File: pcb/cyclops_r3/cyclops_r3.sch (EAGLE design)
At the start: 78 parts, among them Q1 SUM11006, Q2 IRF510, U1 MCP4921, U2 317-N, U3 TLV37, U4 337-N, U5 ADR03, U6 OP1177, U7 TLV2374, U8 ZXTD45

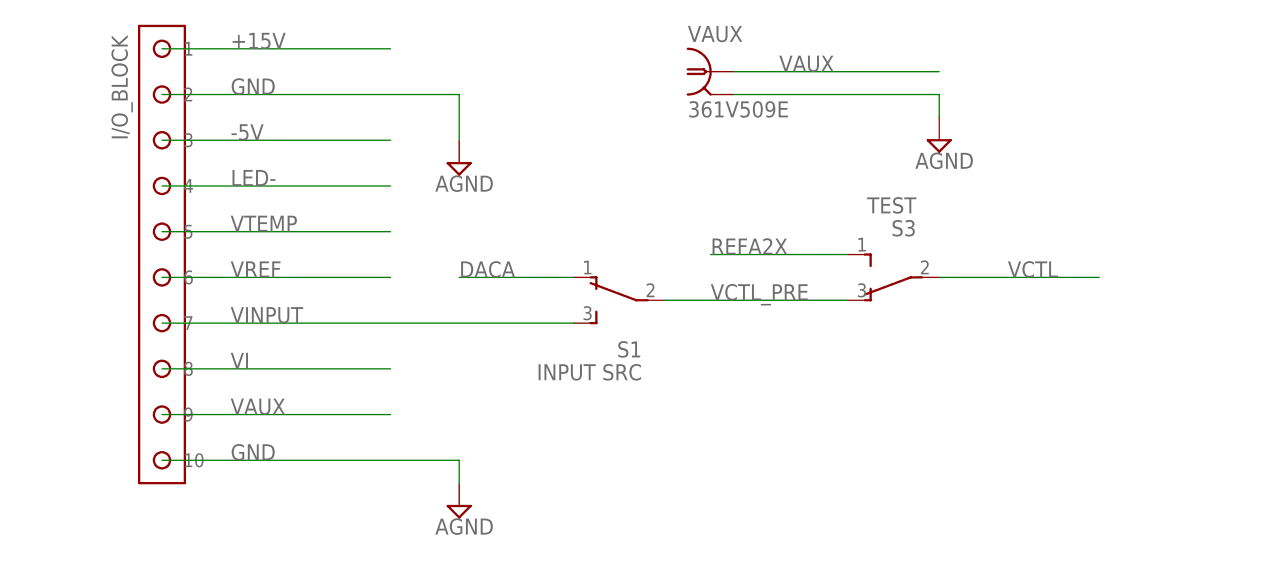
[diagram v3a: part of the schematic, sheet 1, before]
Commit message: Almost done fixing the top/bottom side I/O labels. Also, found a big mistake in the 10-pin screw terminal header: I replaced the +LED supply with the -5V supply rail. I had to shift all the pins to get that LED pin back and I have not finished rerouting the board.
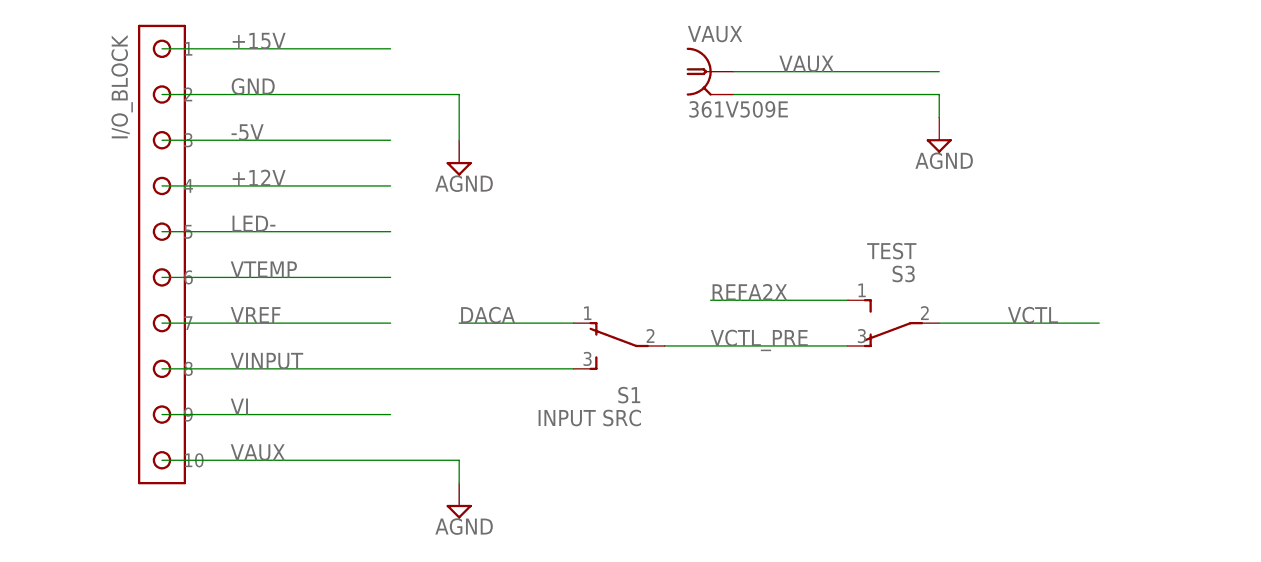
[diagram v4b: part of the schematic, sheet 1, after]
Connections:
- net +12V: now also I/O_BLOCK.4
- net GND: no longer I/O_BLOCK.10
- net LED-: now also I/O_BLOCK.5; no longer I/O_BLOCK.4
- net VAUX: now also I/O_BLOCK.10; no longer I/O_BLOCK.9
- net VI: now also I/O_BLOCK.9; no longer I/O_BLOCK.8
- net VINPUT: now also I/O_BLOCK.8; no longer I/O_BLOCK.7
- net VREF: now also I/O_BLOCK.7; no longer I/O_BLOCK.6
- net VTEMP: now also I/O_BLOCK.6; no longer I/O_BLOCK.5
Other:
- moved on the sheet: S1, S3
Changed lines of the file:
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@@
 <instance part="SUPPLY32" gate="G$1" x="76.2" y="-17.78"/>
 <instance part="SUPPLY33" gate="G$1" x="76.2" y="-55.88"/>
-<instance part="S1" gate="G$1" x="96.52" y="-33.02" rot="MR0"/>
+<instance part="S1" gate="G$1" x="96.52" y="-38.1" rot="MR0"/>
 <instance part="SUPPLY12" gate="G$1" x="165.1" y="22.86"/>
 <instance part="SUPPLY34" gate="PE" x="139.7" y="22.86"/>
-<instance part="S3" gate="G$1" x="127" y="-30.48" rot="R180"/>
+<instance part="S3" gate="G$1" x="127" y="-35.56" rot="R180"/>
 <instance part="SUPPLY4" gate="PE" x="60.96" y="10.16"/>
 <instance part="SUPPLY29" gate="PE" x="38.1" y="83.82"/>
@@
 <segment>
 <pinref part="S1" gate="G$1" pin="1"/>
-<wire x1="76.2" y1="-30.48" x2="88.9" y2="-30.48" width="0.1524" layer="91"/>
-<label x="76.2" y="-30.48" size="1.778" layer="95"/>
+<wire x1="76.2" y1="-35.56" x2="88.9" y2="-35.56" width="0.1524" layer="91"/>
+<label x="76.2" y="-35.56" size="1.778" layer="95"/>
 </segment>
 </net>
@@
 <net name="LED-" class="0">
 <segment>
-<pinref part="I/O_BLOCK" gate="G$1" pin="4"/>
-<wire x1="43.18" y1="-20.32" x2="68.58" y2="-20.32" width="0.1524" layer="91"/>
-<label x="50.8" y="-20.32" size="1.778" layer="95"/>
+<pinref part="I/O_BLOCK" gate="G$1" pin="5"/>
+<wire x1="43.18" y1="-25.4" x2="68.58" y2="-25.4" width="0.1524" layer="91"/>
+<label x="50.8" y="-25.4" size="1.778" layer="95"/>
 </segment>
 </net>
@@
 </segment>
 <segment>
-<pinref part="I/O_BLOCK" gate="G$1" pin="10"/>
-<wire x1="43.18" y1="-50.8" x2="76.2" y2="-50.8" width="0.1524" layer="91"/>
-<pinref part="SUPPLY33" gate="G$1" pin="AGND"/>
-<wire x1="76.2" y1="-50.8" x2="76.2" y2="-53.34" width="0.1524" layer="91"/>
-<label x="50.8" y="-50.8" size="1.778" layer="95"/>
-</segment>
-<segment>
 <pinref part="C1" gate="C" pin="2"/>
 <pinref part="SUPPLY16" gate="G$1" pin="AGND"/>
@@
 <net name="VAUX" class="0">
 <segment>
+<pinref part="VAUX" gate="G$1" pin="1"/>
+<wire x1="106.68" y1="-7.62" x2="129.54" y2="-7.62" width="0.1524" layer="91"/>
+<label x="111.76" y="-7.62" size="1.778" layer="95"/>
+</segment>
+<segment>
+<pinref part="I/O_BLOCK" gate="G$1" pin="10"/>
+<wire x1="43.18" y1="-50.8" x2="76.2" y2="-50.8" width="0.1524" layer="91"/>
+<pinref part="SUPPLY33" gate="G$1" pin="AGND"/>
+<wire x1="76.2" y1="-50.8" x2="76.2" y2="-53.34" width="0.1524" layer="91"/>
+<label x="50.8" y="-50.8" size="1.778" layer="95"/>
+</segment>
+</net>
+<net name="VI" class="0">
+<segment>
 <pinref part="I/O_BLOCK" gate="G$1" pin="9"/>
 <wire x1="43.18" y1="-45.72" x2="68.58" y2="-45.72" width="0.1524" layer="91"/>
 <label x="50.8" y="-45.72" size="1.778" layer="95"/>
 </segment>
-<segment>
-<pinref part="VAUX" gate="G$1" pin="1"/>
-<wire x1="106.68" y1="-7.62" x2="129.54" y2="-7.62" width="0.1524" layer="91"/>
-<label x="111.76" y="-7.62" size="1.778" layer="95"/>
-</segment>
-</net>
-<net name="VI" class="0">
+</net>
+<net name="VINPUT" class="0">
 <segment>
 <pinref part="I/O_BLOCK" gate="G$1" pin="8"/>
-<wire x1="43.18" y1="-40.64" x2="68.58" y2="-40.64" width="0.1524" layer="91"/>
+<wire x1="43.18" y1="-40.64" x2="88.9" y2="-40.64" width="0.1524" layer="91"/>
 <label x="50.8" y="-40.64" size="1.778" layer="95"/>
-</segment>
-</net>
-<net name="VINPUT" class="0">
-<segment>
-<pinref part="I/O_BLOCK" gate="G$1" pin="7"/>
-<label x="50.8" y="-35.56" size="1.778" layer="95"/>
 <pinref part="S1" gate="G$1" pin="3"/>
-<wire x1="43.18" y1="-35.56" x2="88.9" y2="-35.56" width="0.1524" layer="91"/>
 </segment>
 </net>
@@
 <net name="VTEMP" class="0">
 <segment>
-<pinref part="I/O_BLOCK" gate="G$1" pin="5"/>
-<wire x1="43.18" y1="-25.4" x2="68.58" y2="-25.4" width="0.1524" layer="91"/>
-<label x="50.8" y="-25.4" size="1.778" layer="95"/>
+<pinref part="I/O_BLOCK" gate="G$1" pin="6"/>
+<wire x1="43.18" y1="-30.48" x2="68.58" y2="-30.48" width="0.1524" layer="91"/>
+<label x="50.8" y="-30.48" size="1.778" layer="95"/>
 </segment>
 </net>
@@
 <net name="VCTL_PRE" class="0">
 <segment>
-<wire x1="99.06" y1="-33.02" x2="119.38" y2="-33.02" width="0.1524" layer="91"/>
+<wire x1="99.06" y1="-38.1" x2="119.38" y2="-38.1" width="0.1524" layer="91"/>
 <pinref part="S1" gate="G$1" pin="2"/>
+<label x="104.14" y="-38.1" size="1.778" layer="95"/>
+<pinref part="S3" gate="G$1" pin="1"/>
+</segment>
+</net>
+<net name="VCTL" class="0">
+<segment>
+<pinref part="S3" gate="G$1" pin="2"/>
+<wire x1="129.54" y1="-35.56" x2="147.32" y2="-35.56" width="0.1524" layer="91"/>
+<label x="137.16" y="-35.56" size="1.778" layer="95"/>
+</segment>
+</net>
+<net name="REFA2X" class="0">
+<segment>
+<pinref part="S3" gate="G$1" pin="3"/>
+<wire x1="119.38" y1="-33.02" x2="104.14" y2="-33.02" width="0.1524" layer="91"/>
 <label x="104.14" y="-33.02" size="1.778" layer="95"/>
-<pinref part="S3" gate="G$1" pin="1"/>
-</segment>
-</net>
-<net name="VCTL" class="0">
-<segment>
-<pinref part="S3" gate="G$1" pin="2"/>
-<wire x1="129.54" y1="-30.48" x2="147.32" y2="-30.48" width="0.1524" layer="91"/>
-<label x="137.16" y="-30.48" size="1.778" layer="95"/>
-</segment>
-</net>
-<net name="REFA2X" class="0">
-<segment>
-<pinref part="S3" gate="G$1" pin="3"/>
-<wire x1="119.38" y1="-27.94" x2="104.14" y2="-27.94" width="0.1524" layer="91"/>
-<label x="104.14" y="-27.94" size="1.778" layer="95"/>
 </segment>
 </net>
 <net name="VREF" class="0">
 <segment>
-<pinref part="I/O_BLOCK" gate="G$1" pin="6"/>
-<wire x1="43.18" y1="-30.48" x2="68.58" y2="-30.48" width="0.1524" layer="91"/>
-<label x="50.8" y="-30.48" size="1.778" layer="95"/>
+<wire x1="43.18" y1="-35.56" x2="68.58" y2="-35.56" width="0.1524" layer="91"/>
+<pinref part="I/O_BLOCK" gate="G$1" pin="7"/>
+<label x="50.8" y="-35.56" size="1.778" layer="95"/>
 </segment>
 </net>
@@
 </segment>
 </net>
+<net name="+12V" class="1">
+<segment>
+<pinref part="I/O_BLOCK" gate="G$1" pin="4"/>
+<wire x1="43.18" y1="-20.32" x2="68.58" y2="-20.32" width="0.1524" layer="91"/>
+<label x="50.8" y="-20.32" size="1.778" layer="95"/>
+</segment>
+</net>

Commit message: Board sent to fab house. Doing some directory clean up now.
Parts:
- Q2: value IRF510 -> IRF540
- S4: value UNKILL -> REVIVE
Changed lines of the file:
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@@
 <part name="I/O_BLOCK" library="cyclops" deviceset="SCREW10" device="_0.1-THRU"/>
 <part name="SUPPLY32" library="cyclops" deviceset="AGND" device=""/>
-<part name="SUPPLY33" library="cyclops" deviceset="AGND" device=""/>
 <part name="S1" library="cyclops" deviceset="SPDT" device="_PCM12" value="INPUT SRC"/>
 <part name="C17" library="cyclops" deviceset="C" device="_0603" value=".1uF"/>
@@
 <part name="U8" library="cyclops" deviceset="ZXTD4591E6" device="" value="ZXTD45"/>
 <part name="SUPPLY35" library="cyclops" deviceset="AGND" device=""/>
-<part name="Q2" library="cyclops" deviceset="N-MOSFET" device="TO-262" value="IRF510"/>
+<part name="Q2" library="cyclops" deviceset="N-MOSFET" device="TO-262" value="IRF540"/>
 <part name="R23" library="cyclops" deviceset="R" device="_0603" value="10"/>
 <part name="R24" library="cyclops" deviceset="R" device="_0603" value="1k"/>
@@
 <part name="C5" library="cyclops" deviceset="C" device="_0603" value="10nF"/>
 <part name="SUPPLY45" library="cyclops" deviceset="AGND" device=""/>
-<part name="S4" library="cyclops" deviceset="SPST_TACT" device="-EVQQ2" value="UNKILL"/>
+<part name="S4" library="cyclops" deviceset="SPST_TACT" device="-EVQQ2" value="REVIVE"/>
 <part name="SUPPLY46" library="supply2" deviceset="AGND" device=""/>
 <part name="U4" library="cyclops" deviceset="*337" device="IMP" value="337-N"/>
@@
 </instance>
 <instance part="SUPPLY32" gate="G$1" x="76.2" y="-17.78"/>
-<instance part="SUPPLY33" gate="G$1" x="76.2" y="-55.88"/>
 <instance part="S1" gate="G$1" x="96.52" y="-38.1" rot="MR0"/>
 <instance part="SUPPLY12" gate="G$1" x="165.1" y="22.86"/>
@@
 <segment>
 <pinref part="I/O_BLOCK" gate="G$1" pin="10"/>
-<wire x1="43.18" y1="-50.8" x2="76.2" y2="-50.8" width="0.1524" layer="91"/>
-<pinref part="SUPPLY33" gate="G$1" pin="AGND"/>
-<wire x1="76.2" y1="-50.8" x2="76.2" y2="-53.34" width="0.1524" layer="91"/>
+<wire x1="43.18" y1="-50.8" x2="68.58" y2="-50.8" width="0.1524" layer="91"/>
 <label x="50.8" y="-50.8" size="1.778" layer="95"/>
 </segment>

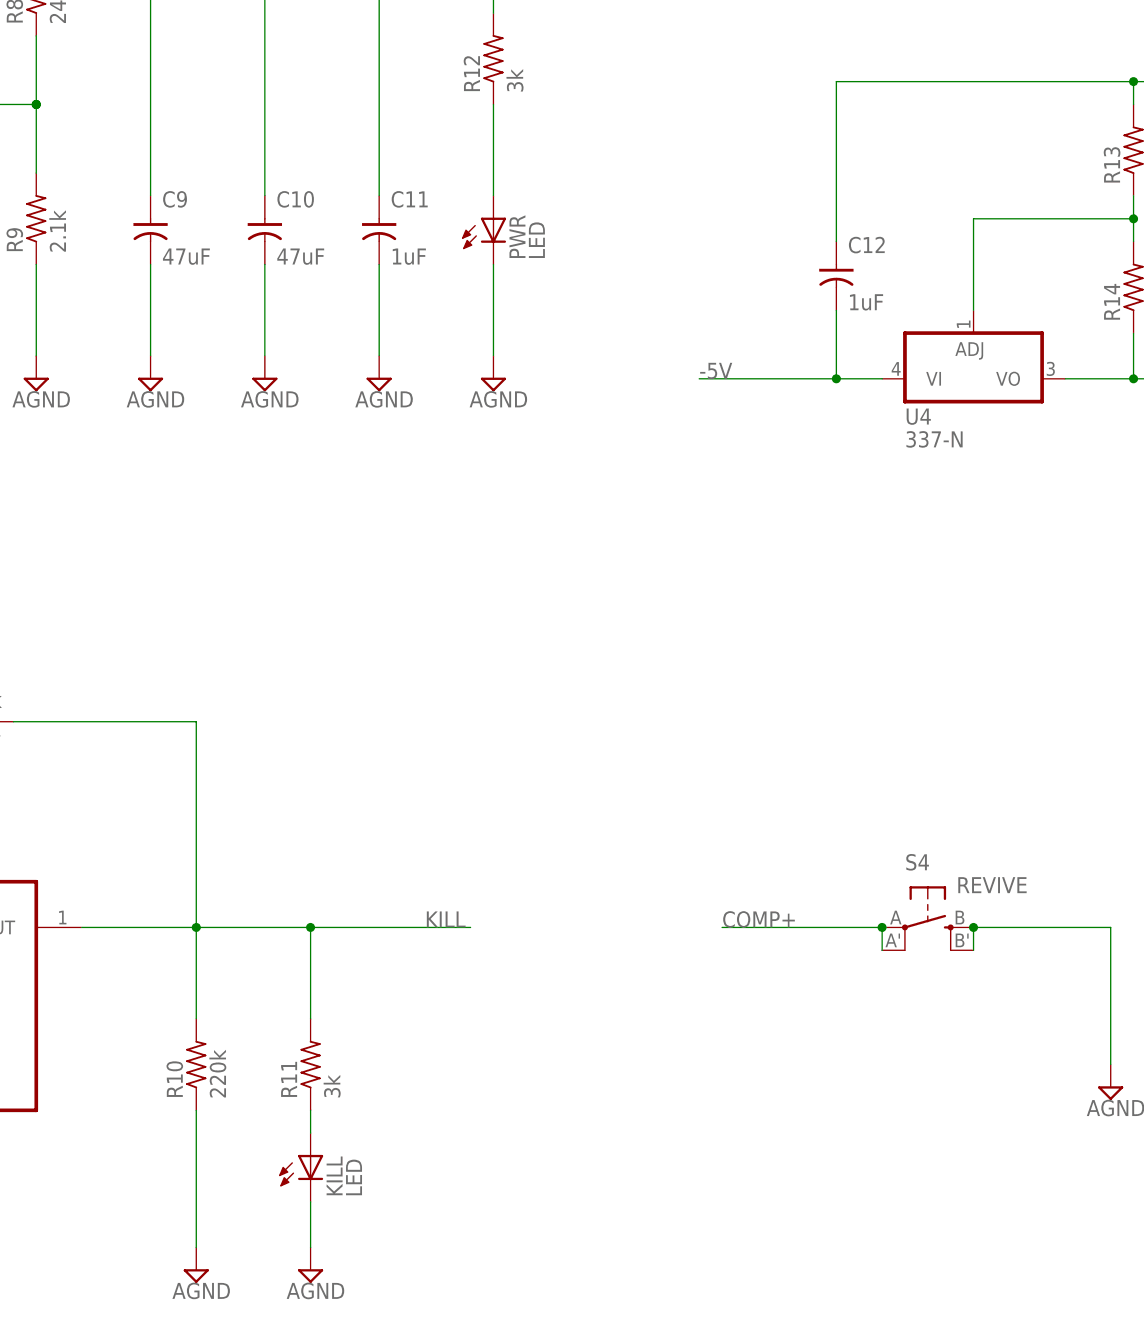
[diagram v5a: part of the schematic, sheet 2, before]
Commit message: Finished up the BOM. Cleaned up the eagle library a bit.
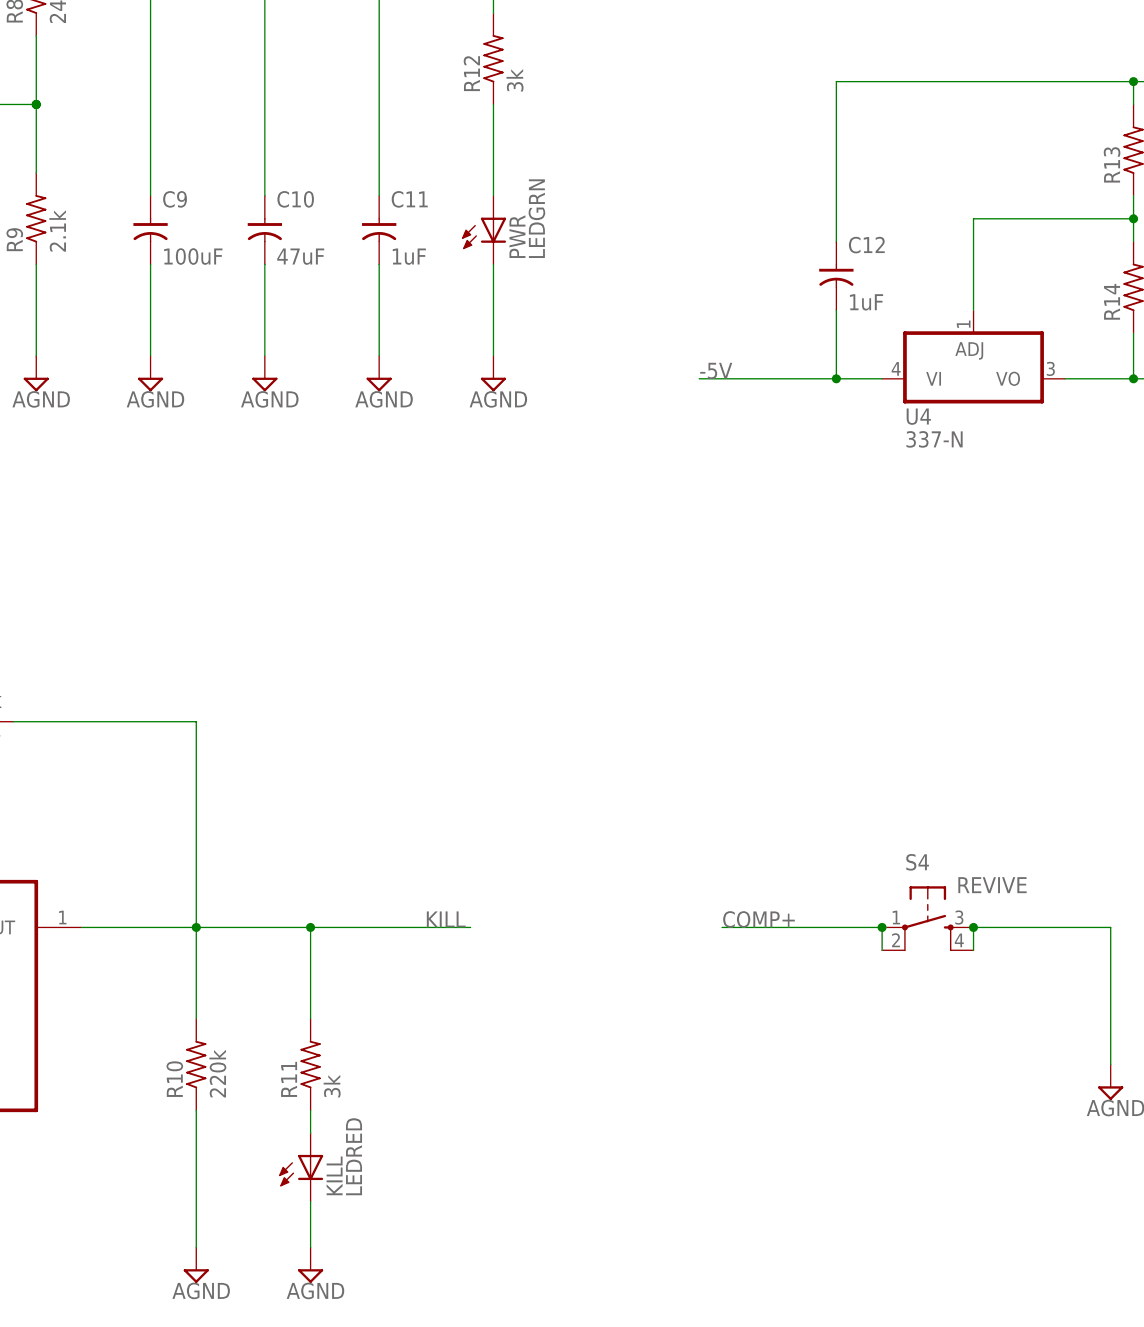
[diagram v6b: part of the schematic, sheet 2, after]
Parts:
- C1, C21, R1: value ?? -> (none)
- C9: value 47uF -> 100uF
- KILL: value LED -> LEDRED
- PWR: value LED -> LEDGRN
- S4: device cyclops:SPST_TACT-EVQQ2 -> jonnew-eagle:SPST_TACT-B3F
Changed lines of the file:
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@@
 <part name="SUPPLY15" library="cyclops" deviceset="GND" device=""/>
 <part name="S2" library="cyclops" deviceset="219-04*" device=""/>
-<part name="C1" library="cyclops" deviceset="C" device="_0603" value="??"/>
-<part name="R1" library="cyclops" deviceset="R" device="_0603" value="??"/>
+<part name="C1" library="cyclops" deviceset="C" device="_0603"/>
+<part name="R1" library="cyclops" deviceset="R" device="_0603"/>
 <part name="SUPPLY16" library="cyclops" deviceset="AGND" device=""/>
 <part name="R22" library="cyclops" deviceset="R" device="_0603" value="9k"/>
@@
 <part name="C17" library="cyclops" deviceset="C" device="_0603" value=".1uF"/>
 <part name="C15" library="cyclops" deviceset="C" device="_0805" value="1uF"/>
-<part name="C9" library="cyclops" deviceset="C-POL" device="_0807" value="47uF"/>
+<part name="C9" library="cyclops" deviceset="C-POL" device="_0807" value="100uF"/>
 <part name="SUPPLY31" library="cyclops" deviceset="AGND" device=""/>
 <part name="SUPPLY12" library="cyclops" deviceset="AGND" device=""/>
@@
 <part name="VGATE" library="cyclops" deviceset="TP" device="TP08R"/>
 <part name="R12" library="cyclops" deviceset="R" device="_0603" value="3k"/>
-<part name="PWR" library="cyclops" deviceset="LED" device="_0805" technology="GREEN" value="LED"/>
+<part name="PWR" library="cyclops" deviceset="LED" device="_0805" technology="GREEN" value="LEDGRN"/>
 <part name="SUPPLY40" library="supply2" deviceset="AGND" device=""/>
 <part name="R10" library="cyclops" deviceset="R" device="_0603" value="220k"/>
@@
 <part name="SUPPLY43" library="cyclops" deviceset="AGND" device=""/>
 <part name="R11" library="cyclops" deviceset="R" device="_0603" value="3k"/>
-<part name="KILL" library="cyclops" deviceset="LED" device="_0805" technology="RED" value="LED"/>
+<part name="KILL" library="cyclops" deviceset="LED" device="_0805" technology="RED" value="LEDRED"/>
 <part name="SUPPLY44" library="supply2" deviceset="AGND" device=""/>
 <part name="C5" library="cyclops" deviceset="C" device="_0603" value="10nF"/>
 <part name="SUPPLY45" library="cyclops" deviceset="AGND" device=""/>
-<part name="S4" library="cyclops" deviceset="SPST_TACT" device="-EVQQ2" value="REVIVE"/>
+<part name="S4" library="jonnew-eagle" deviceset="SPST_TACT" device="-B3F" value="REVIVE"/>
 <part name="SUPPLY46" library="supply2" deviceset="AGND" device=""/>
 <part name="U4" library="cyclops" deviceset="*337" device="IMP" value="337-N"/>
@@
 <part name="-2.1V1" library="cyclops" deviceset="-5V" device="" value="-2.1V"/>
 <part name="-2.1V2" library="cyclops" deviceset="-5V" device="" value="-2.1V"/>
-<part name="C21" library="cyclops" deviceset="C" device="_0603" value="??"/>
+<part name="C21" library="cyclops" deviceset="C" device="_0603"/>
 </parts>
 <sheets>

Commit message: Fixed the pads of the RSense resistor.
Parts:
- RSENSE: device cyclops:R_2512 -> cyclops:R_2512W
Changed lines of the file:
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@@
 <part name="R22" library="cyclops" deviceset="R" device="_0603" value="9k"/>
 <part name="R21" library="cyclops" deviceset="R" device="_0603" value="1k"/>
-<part name="RSENSE" library="cyclops" deviceset="R" device="_2512" value="0.1,1W"/>
+<part name="RSENSE" library="cyclops" deviceset="R" device="_2512W" value="0.1,1W"/>
 <part name="U5" library="cyclops" deviceset="ADR03AKSZ-REEL7" device="" value="ADR03"/>
 <part name="C14" library="cyclops" deviceset="C" device="_0805" value="1uF"/>

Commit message: Fixes to the BOM.
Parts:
- R21: value 1k -> 1k 0.1%
- R22: value 9k -> 9k 0.1%
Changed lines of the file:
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@@
 <part name="R1" library="cyclops" deviceset="R" device="_0603"/>
 <part name="SUPPLY16" library="cyclops" deviceset="AGND" device=""/>
-<part name="R22" library="cyclops" deviceset="R" device="_0603" value="9k"/>
-<part name="R21" library="cyclops" deviceset="R" device="_0603" value="1k"/>
+<part name="R22" library="cyclops" deviceset="R" device="_0603" value="9k 0.1%"/>
+<part name="R21" library="cyclops" deviceset="R" device="_0603" value="1k 0.1%"/>
 <part name="RSENSE" library="cyclops" deviceset="R" device="_2512W" value="0.1,1W"/>
 <part name="U5" library="cyclops" deviceset="ADR03AKSZ-REEL7" device="" value="ADR03"/>
